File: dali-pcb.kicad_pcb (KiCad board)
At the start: 2 copper layers, 180.5 x 113 mm, 62 parts, among them J1 12-22.5V DC, J10 5V DC, J11 5V DC, J12 5V DC, J13 5V DC, J14 5V DC, J15 GND, J2 DALI BUS, J20 LOLIN-S3 (L), J21 LOLIN-S3 (R), J22 ESP32-S3-DEVKITC-1 (L), J23 ESP32-S3-DEVKITC-1 (R), J24 LOLIN-S3-MINI (L), J25 LOLIN-S3-MINI (R), J26 LOLIN-S2-MINI (L), J27 LOLIN-S2-MINI (R), J3 DALI BUS, J30 FTDI-MCU, J31 UART-DALI, J4 DALI BUS, J40 A10-0, J41 A5-0, J42 A5-5, J43 A2-0, J44 A2-2, J45 A2-4, J46 A2-6, J47 A2-8, J50 D8-11, J51 D4-11, J52 D4-16, J53 D2-11, J54 D2-13, J55 D2-16, J56 D2-18, J60 D1-11, J61 D1-12, J62 D1-13, J63 D1-14, Q1 PZT2222A, Q2 MMBT2222A, U1 TCLT1000, U2 TCLT1000

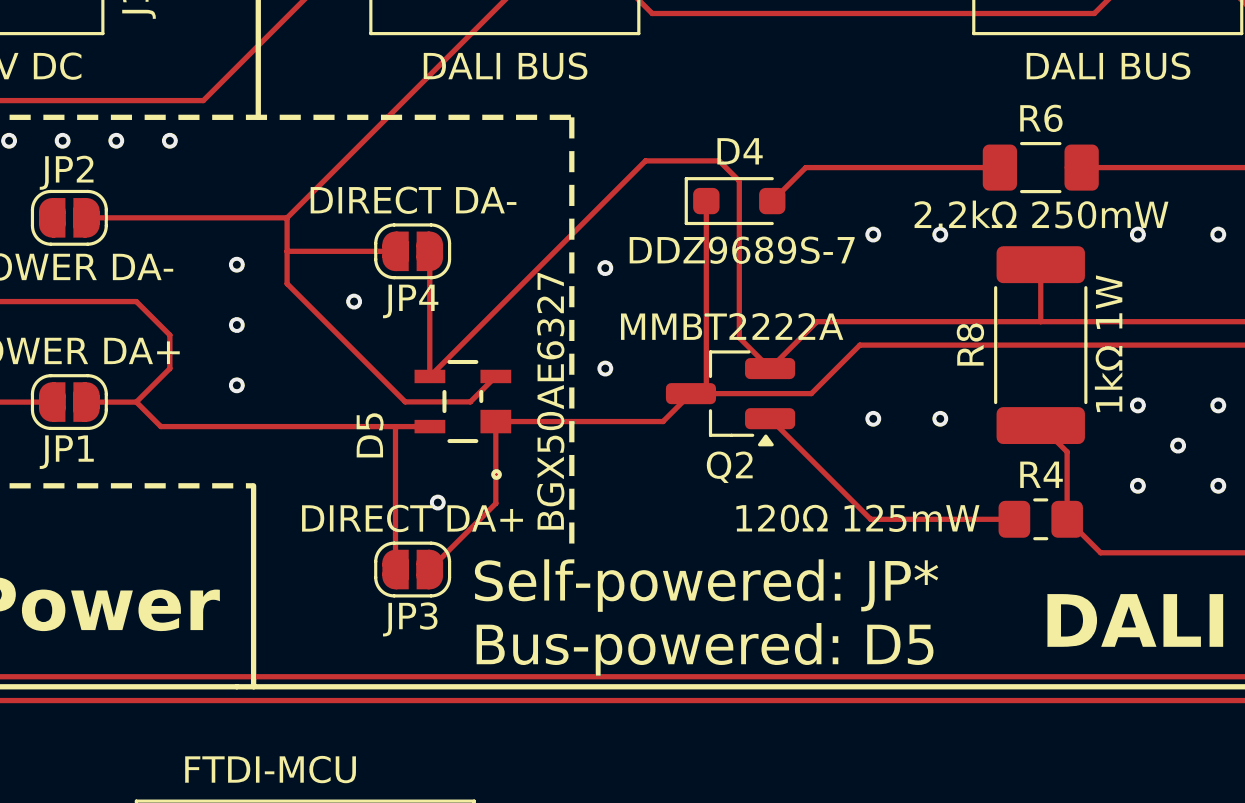
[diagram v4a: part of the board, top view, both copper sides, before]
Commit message: Move D5/JP3/JP4 to improve silkscreen position
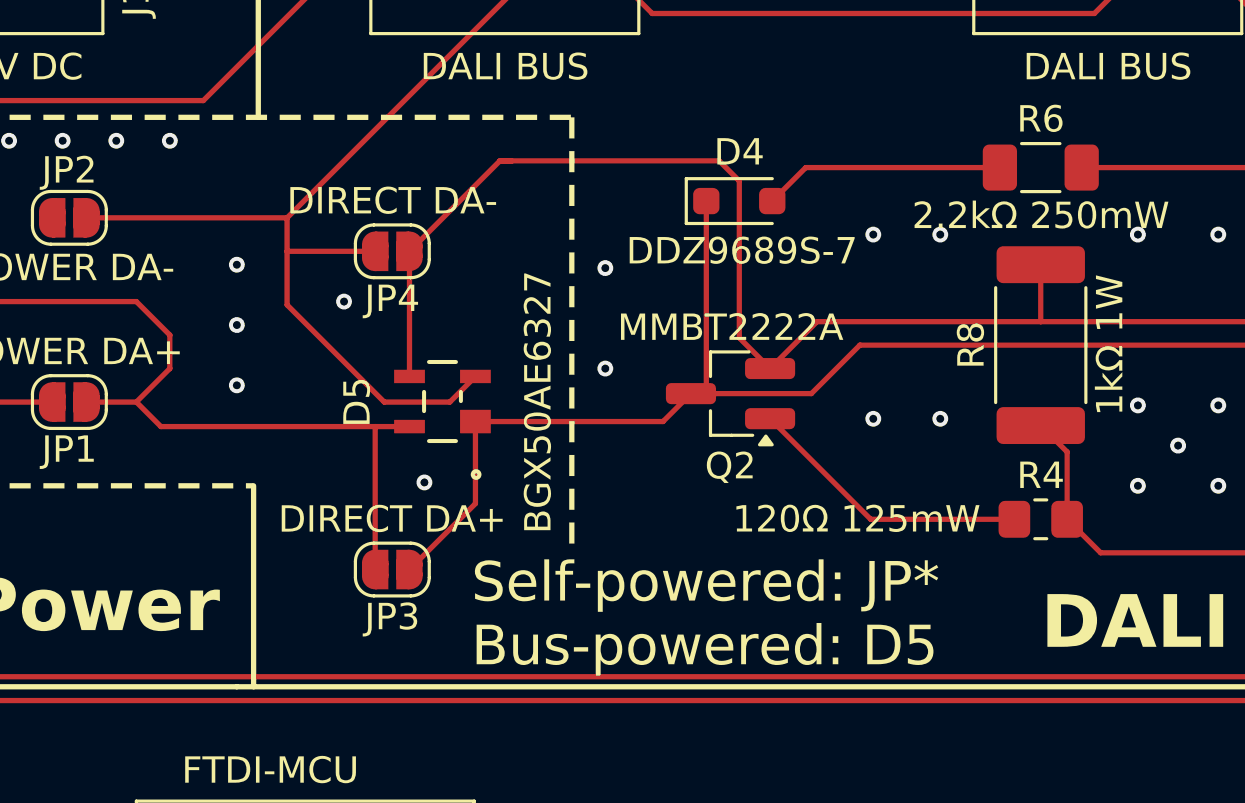
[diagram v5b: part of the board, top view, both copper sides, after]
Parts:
- moved D5 0.77 mm to (56.1, 39.3)
- moved JP3 0.77 mm to (54.2, 45.7)
- moved JP4 0.77 mm to (54.2, 33.7)
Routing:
- net /DALI/DA-: track 90.4 -> 89.4 mm
- net /DALI/DA+: track 111.5 -> 110.7 mm
- net Net-(D4-K): track 56.4 -> 57.2 mm
- net Net-(D5--): track 51.8 -> 51.0 mm
- net Net-(R6-Pad2): track 9.39 -> 8.76 mm
- net Net-(D4-A): track 9.79 -> 9.16 mm
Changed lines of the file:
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@@
 		(placed yes)
 		(layer "F.Cu")
-		(at 56.830001 39.349599 90)
+		(at 56.056306 39.349599 90)
 		(tags "BGX50AE6327HTSA1 ")
 		(property "Reference" "D5"
-			(at -1.290401 -3.490001 90)
+			(at -0.020401 -3.224306 90)
 			(unlocked yes)
 			(layer "F.SilkS")
@@
 		)
 		(property "Value" "BGX50AE6327"
-			(at 0 3.367999 90)
+			(at -0.020401 3.633694 90)
 			(unlocked yes)
 			(layer "F.SilkS")
@@
 	(footprint "Jumper:SolderJumper-2_P1.3mm_Open_RoundedPad1.0x1.5mm"
 		(layer "F.Cu")
-		(at 54.9252 33.655 180)
+		(at 54.155 33.655 180)
 		(descr "SMD Solder Jumper, 1x1.5mm, rounded Pads, 0.3mm gap, open")
 		(tags "solder jumper open")
@@
 	(footprint "Jumper:SolderJumper-2_P1.3mm_Open_RoundedPad1.0x1.5mm"
 		(layer "F.Cu")
-		(at 54.9252 45.72 180)
+		(at 54.155 45.72 180)
 		(descr "SMD Solder Jumper, 1x1.5mm, rounded Pads, 0.3mm gap, open")
 		(tags "solder jumper open")
@@
 	)
 	(segment
-		(start 77.105 30.48)
-		(end 77.74 30.48)
-		(width 0.2)
-		(layer "F.Cu")
-		(net 4)
-	)
-	(segment
 		(start 69.83 30.48)
 		(end 77.19 30.48)
@@
 	)
 	(segment
-		(start 58.079601 43.215599)
-		(end 58.079601 40.109099)
+		(start 66.04 39.05)
+		(end 70.043 39.05)
 		(width 0.2)
 		(layer "F.Cu")
@@
 	)
 	(segment
-		(start 66.04 39.05)
-		(end 70.043 39.05)
+		(start 54.805 45.72)
+		(end 57.305906 43.219094)
 		(width 0.2)
 		(layer "F.Cu")
@@
 	)
 	(segment
-		(start 55.5752 45.72)
-		(end 58.079601 43.215599)
+		(start 57.305906 40.109099)
+		(end 64.418401 40.109099)
 		(width 0.2)
 		(layer "F.Cu")
@@
 	)
 	(segment
-		(start 58.079601 40.109099)
-		(end 64.418401 40.109099)
+		(start 71.882 37.211)
+		(end 95.377 37.211)
 		(width 0.2)
 		(layer "F.Cu")
@@
 	)
 	(segment
-		(start 71.882 37.211)
-		(end 95.377 37.211)
+		(start 57.305906 43.219094)
+		(end 57.305906 40.109099)
 		(width 0.2)
 		(layer "F.Cu")
@@
 	)
 	(segment
-		(start 55.580402 38.399598)
-		(end 63.754 30.226)
+		(start 58.674 30.226)
+		(end 58.230505 30.226)
 		(width 0.2)
 		(layer "F.Cu")
@@
 	)
 	(segment
-		(start 63.754 30.226)
-		(end 66.548 30.226)
+		(start 68.4775 38.1)
+		(end 67.31 36.9325)
 		(width 0.2)
 		(layer "F.Cu")
@@
 	)
 	(segment
+		(start 67.31 36.9325)
+		(end 67.31 30.988)
+		(width 0.2)
+		(layer "F.Cu")
+		(net 6)
+	)
+	(segment
 		(start 68.4775 38.1)
 		(end 70.2555 36.322)
@@
 	)
 	(segment
-		(start 55.5752 33.655)
-		(end 55.5752 38.394396)
+		(start 58.234 30.226)
+		(end 58.674 30.226)
+		(width 0.2)
+		(layer "F.Cu")
+		(net 6)
+	)
+	(segment
+		(start 54.805 33.655)
+		(end 54.805 38.397891)
 		(width 0.2)
 		(layer "F.Cu")
@@
 	)
 	(segment
-		(start 68.4775 38.1)
-		(end 67.31 36.9325)
+		(start 54.805 33.655)
+		(end 58.234 30.226)
 		(width 0.2)
 		(layer "F.Cu")
@@
 	)
 	(segment
-		(start 66.548 30.226)
-		(end 67.31 30.988)
+		(start 67.31 30.988)
+		(end 66.548 30.226)
 		(width 0.2)
 		(layer "F.Cu")
@@
 	)
 	(segment
-		(start 67.31 30.988)
-		(end 67.31 36.9325)
+		(start 66.548 30.226)
+		(end 58.674 30.226)
 		(width 0.2)
 		(layer "F.Cu")
@@
 	)
 	(segment
-		(start 57.115601 39.363599)
-		(end 58.079601 38.399599)
-		(width 0.2)
-		(layer "F.Cu")
-		(net 7)
-	)
-	(segment
-		(start 54.644401 39.363599)
-		(end 57.115601 39.363599)
+		(start 50.165 32.385)
+		(end 60.96 21.59)
 		(width 0.2)
 		(layer "F.Cu")
@@
 	)
 	(segment
-		(start 50.165 32.385)
-		(end 60.96 21.59)
+		(start 53.848 39.37)
+		(end 50.165 35.687)
 		(width 0.2)
 		(layer "F.Cu")
@@
 	)
 	(segment
-		(start 50.165 34.884198)
-		(end 54.644401 39.363599)
+		(start 56.335505 39.37)
+		(end 53.848 39.37)
 		(width 0.2)
 		(layer "F.Cu")
@@
 	)
 	(segment
-		(start 54.2752 33.655)
-		(end 50.165 33.655)
+		(start 64.008 24.638)
+		(end 80.772 24.638)
 		(width 0.2)
 		(layer "F.Cu")
@@
 	)
 	(segment
-		(start 64.008 24.638)
-		(end 80.772 24.638)
+		(start 57.305906 38.399599)
+		(end 56.335505 39.37)
 		(width 0.2)
 		(layer "F.Cu")
@@
 	)
 	(segment
-		(start 50.165 33.655)
-		(end 50.165 34.884198)
+		(start 50.165 32.385)
+		(end 50.165 33.655)
 		(width 0.2)
 		(layer "F.Cu")
@@
 	)
 	(segment
-		(start 50.165 32.385)
+		(start 50.165 35.687)
+		(end 50.165 33.655)
+		(width 0.2)
+		(layer "F.Cu")
+		(net 7)
+	)
+	(segment
+		(start 53.505 33.655)
 		(end 50.165 33.655)
 		(width 0.2)
@@
 	)
 	(segment
-		(start 81.28 19.05)
-		(end 99.06 19.05)
+		(start 45.3796 40.2996)
+		(end 53.51 40.2996)
 		(width 0.2)
 		(layer "F.Cu")
@@
 	)
 	(segment
-		(start 54.2752 40.3042)
-		(end 54.2798 40.2996)
+		(start 81.28 19.05)
+		(end 99.06 19.05)
 		(width 0.2)
 		(layer "F.Cu")
@@
 	)
 	(segment
-		(start 54.2752 45.72)
-		(end 54.2752 40.3042)
+		(start 53.51 40.2996)
+		(end 54.806707 40.2996)
 		(width 0.2)
 		(layer "F.Cu")
@@
 	)
 	(segment
-		(start 54.2798 40.2996)
-		(end 45.3796 40.2996)
+		(start 55.88 21.59)
+		(end 58.42 19.05)
 		(width 0.2)
 		(layer "F.Cu")
@@
 	)
 	(segment
-		(start 55.88 21.59)
-		(end 58.42 19.05)
+		(start 53.51 40.2996)
+		(end 53.505 40.3046)
 		(width 0.2)
 		(layer "F.Cu")
@@
 	)
 	(segment
-		(start 55.580402 40.2996)
-		(end 54.2798 40.2996)
+		(start 53.505 40.3046)
+		(end 53.505 45.72)
 		(width 0.2)
 		(layer "F.Cu")
@@
 	)
 	(via
-		(at 52.705 35.56)
+		(at 52.324 35.56)
 		(size 0.6)
 		(drill 0.3)
@@
 	)
 	(via
-		(at 55.88 43.18)
+		(at 55.372 42.418)
 		(size 0.6)
 		(drill 0.3)
@@
 	)
 	(segment
-		(start 80.375 30.48)
-		(end 79.74 30.48)
-		(width 0.2)
-		(layer "F.Cu")
-		(net 59)
-	)
-	(segment

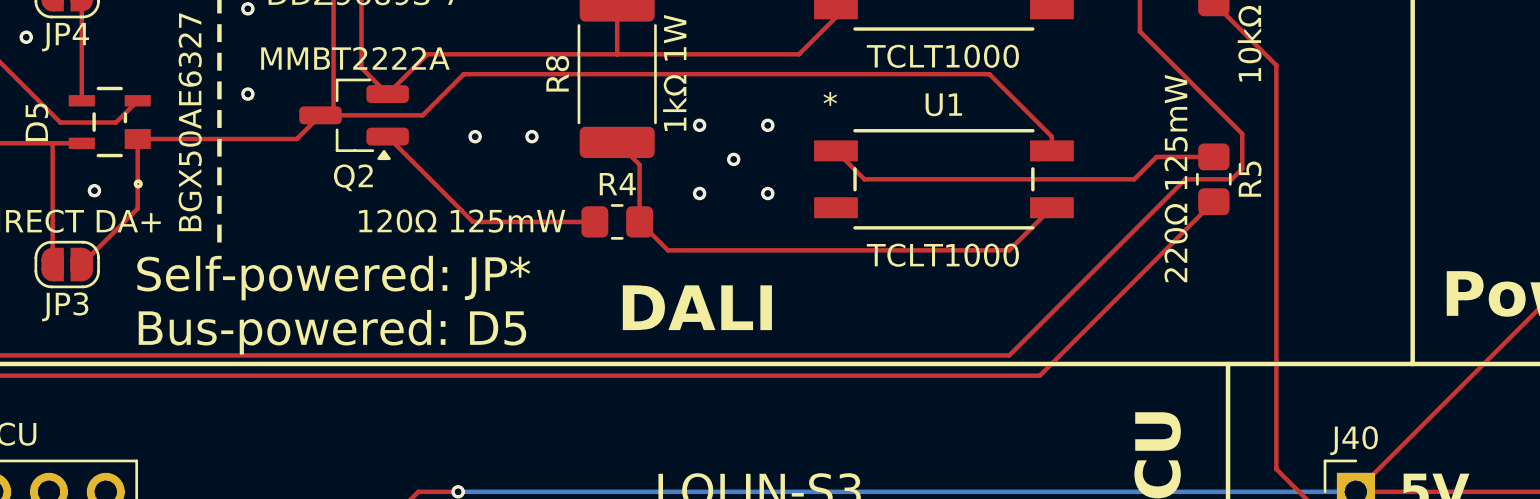
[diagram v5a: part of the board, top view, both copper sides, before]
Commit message: Reword bus power options
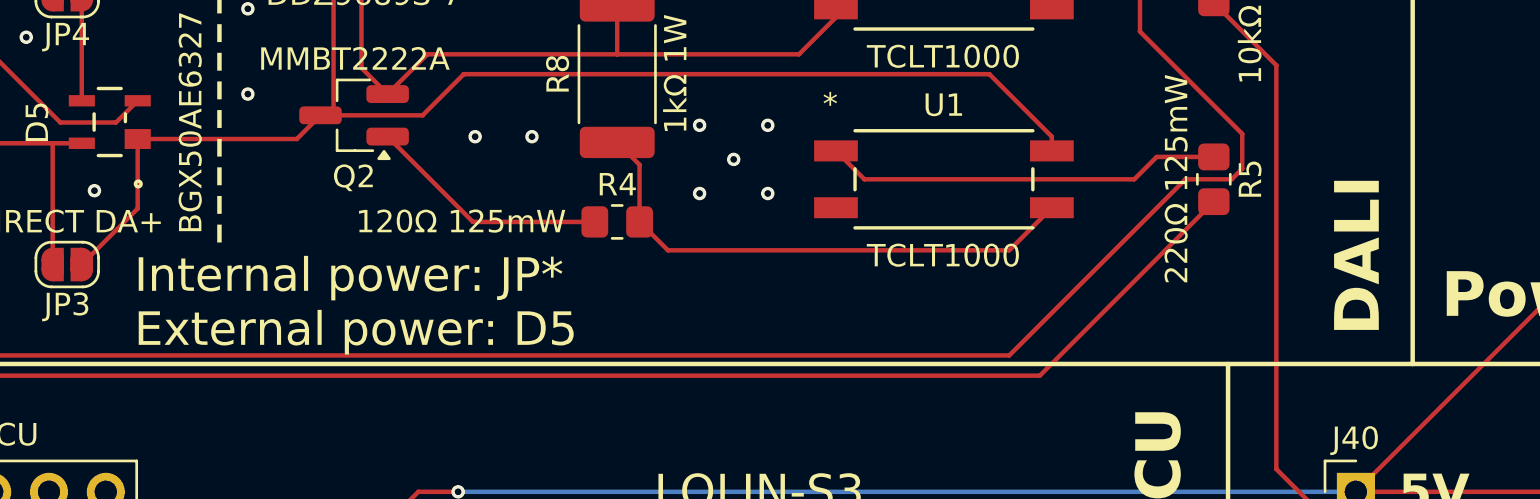
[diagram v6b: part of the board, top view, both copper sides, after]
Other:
- board text added: "Internal power: JP* External power: D5"
- board text removed: "Self-powered: JP* Bus-powered: D5"
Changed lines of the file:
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@@
 			(disableapertmacros no)
 			(usegerberextensions no)
-			(usegerberattributes yes)
-			(usegerberadvancedattributes yes)
-			(creategerberjobfile yes)
+			(usegerberattributes no)
+			(usegerberadvancedattributes no)
+			(creategerberjobfile no)
 			(dashed_line_dash_ratio 12.000000)
 			(dashed_line_gap_ratio 3.000000)
@@
 			(outputformat 1)
 			(mirror no)
-			(drillshape 1)
+			(drillshape 0)
 			(scaleselection 1)
-			(outputdirectory "")
+			(outputdirectory "plots/")
 		)
 	)
@@
 		)
 	)
-	(gr_text "Self-powered: JP*\nBus-powered: D5"
+	(gr_text "Internal power: JP*\nExternal power: D5"
 		(at 57.15 47.4091 0)
 		(layer "F.SilkS" knockout)
@@
 	)
 	(gr_text "DALI"
-		(at 78.74 48.895 0)
+		(at 113.03 48.895 90)
 		(layer "F.SilkS")
 		(effects

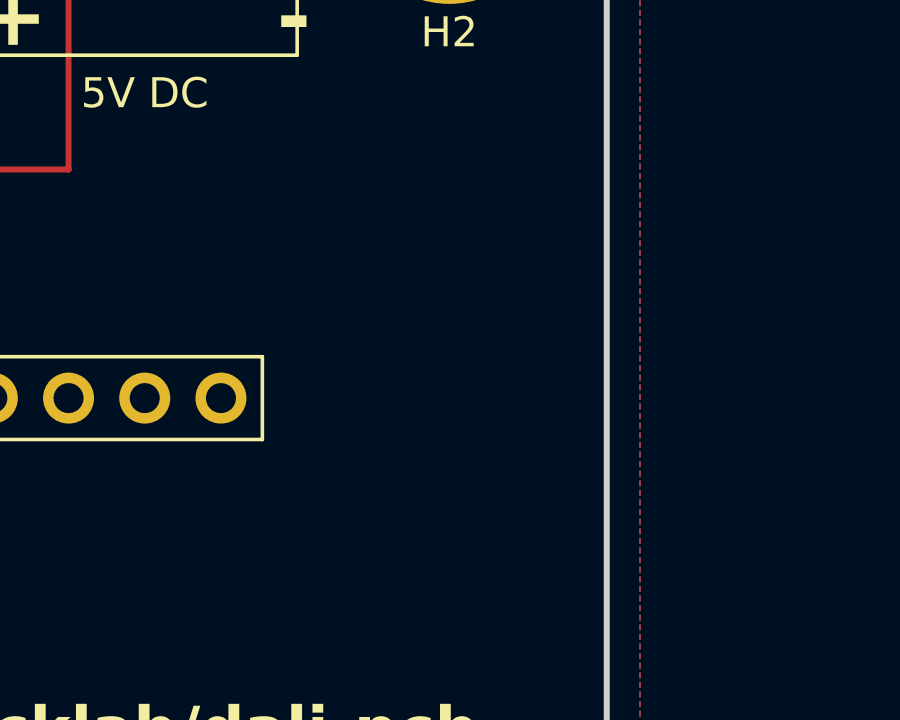
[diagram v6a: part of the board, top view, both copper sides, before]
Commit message: Add JLC text
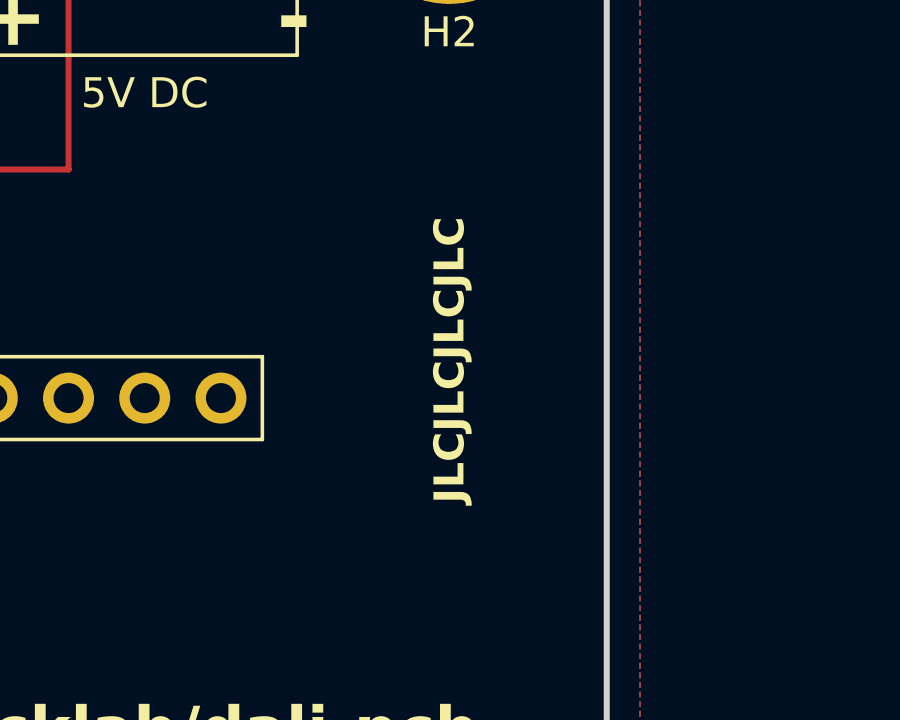
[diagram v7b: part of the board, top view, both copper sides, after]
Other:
- board text added: "JLCJLCJLCJLC"
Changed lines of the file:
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@@
 			(plot_on_all_layers_selection 0x00000000_00000000_00000000_00000000)
 			(disableapertmacros no)
-			(usegerberextensions no)
+			(usegerberextensions yes)
 			(usegerberattributes no)
 			(usegerberadvancedattributes no)
@@
 			(sketchdnponfab yes)
 			(crossoutdnponfab yes)
-			(subtractmaskfromsilk no)
+			(subtractmaskfromsilk yes)
 			(outputformat 1)
 			(mirror no)
@@
 				(bold yes)
 			)
+		)
+	)
+	(gr_text "JLCJLCJLCJLC"
+		(at 190.5 35.56 90)
+		(layer "F.SilkS")
+		(effects
+			(font
+				(size 1 1)
+				(thickness 0.2)
+				(bold yes)
+			)
